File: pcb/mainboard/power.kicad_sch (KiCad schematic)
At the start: 0 parts

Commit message: - pcb: working on power supply
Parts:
- added C? (x3): 10uF, symbol Device:C
- added C? (x3): 22uF, Capacitor_SMD:C_0603_1608Metric, symbol Device:C
- added C? (x6): 100nF, symbol Device:C
- added C? (x3): 22uF, symbol Device:C
- added L? (x3): 470nH, symbol Device:L
- added R? (x3): 100R, Resistor_SMD:R_0402_1005Metric, symbol Device:R
- added R? (x2): 0R, Resistor_SMD:R_0402_1005Metric, symbol Device:R
- added R? (x2): 9.1K, Resistor_SMD:R_0402_1005Metric, symbol Device:R
- added R? (x3): 0.02R, Resistor_SMD:R_0805_2012Metric, symbol Device:R
- added U? (x3): RK809, symbol symbols:RK809
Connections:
- new net: C?.1, C?.1, C?.1, L?.2, R?.1, R?.1
- new net: C?.1, C?.1, U?.24 (VCC3), U?.66 (VCC4)
- new net: C?.2, U?.10 (VCC2), U?.11 (VCC1)
- new net: L?.2, U?.12 (SW1)
- new net: R?.2, R?.2, U?.13 (FB1)
- new net: C?.1, C?.2, R?.2, R?.2, U?.64 (FB4)
- new net: L?.1, U?.65 (SW4)
- new net: R?.2, R?.2, U?.8 (FB2)
- new net: L?.2, U?.9 (SW2)
- new net: C?.1, C?.1, C?.1, L?.1, R?.1, R?.2 (x2)
- new net: C?.1, C?.2, R?.1, R?.1, R?.2 (x2)
- new net GND: C?.1, C?.2, C?.2, C?.2, C?.2, C?.2, C?.2, C?.2, C?.2, C?.2, R?.1, R?.1

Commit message: - Upgrade KiCad to latest version - Working on PM circuits - Initial USB Type-C support - Initial support for LCD
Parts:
- removed R?: 9.1K, Resistor_SMD:R_0402_1005Metric, symbol Device:R
- removed R?: 0R, Resistor_SMD:R_0402_1005Metric, symbol Device:R
- added BT?: Battery, symbol Device:Battery
- added C? (x14): 100nF, Capacitor_SMD:C_0402_1005Metric, symbol Device:C
- added C? (x4): 1uF, symbol Device:C
- added C?: 100nF/16V, Capacitor_SMD:C_0402_1005Metric, symbol Device:C
- added C? (x2): 22uF, symbol Device:C
- added C? (x2): 22pF, Capacitor_SMD:C_0402_1005Metric, symbol Device:C
- added C? (x3): 10uF, symbol Device:C
- added C?: 1uF, Capacitor_SMD:C_0402_1005Metric, symbol Device:C
- added C? (x3): 100nF, symbol Device:C
- added L? (x2): 470nH, symbol Device:L
- added R?: 22K, Resistor_SMD:R_0402_1005Metric, symbol Device:R
- added R?: 120K/1%, Resistor_SMD:R_0402_1005Metric, symbol Device:R
- added R? (x5): 22R, Resistor_SMD:R_0402_1005Metric, symbol Device:R
- added R? (x13): 0.02R, Resistor_SMD:R_0805_2012Metric, symbol Device:R
- added R?: 140K, Resistor_SMD:R_0805_2012Metric, symbol Device:R
- added R?: 0.01R, Resistor_SMD:R_0402_1005Metric, symbol Device:R
- added R? (x2): 10K, Resistor_SMD:R_0402_1005Metric, symbol Device:R
- added R?: 220K, Resistor_SMD:R_0402_1005Metric, symbol Device:R
- added R?: 47K/1%, Resistor_SMD:R_0402_1005Metric, symbol Device:R
- added R?: 20K, Resistor_SMD:R_0402_1005Metric, symbol Device:R
- added SW? (x2): SW_Push, symbol Switch:SW_Push
- added Y?: 32.768K, Crystal:Crystal_SMD_TXC_9HT11-2Pin_2.0x1.2mm_HandSoldering, symbol Device:Crystal
- R?: value 0R -> 560R
- R?: value 9.1K -> DNP
- U?: value RK809 -> RK809-5
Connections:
- net GND: now also C?.2, C?.2, U?.47 (GNDREF), U?.63 (SNSN), U?.69 (EPAD), C?.1, C?.1, C?.1, C?.1, C?.1, C?.2, C?.2, C?.2, C?.2, C?.2, C?.2, C?.2, C?.2, C?.2, C?.2, C?.2, C?.2, C?.2, C?.2, C?.2, C?.2, C?.2, C?.2, C?.2, C?.2, C?.2, C?.2, C?.2, C?.2, C?.2, R?.2, R?.2, R?.2, R?.2, SW?.2, SW?.2
- net +3V3_SYS: now reaches C?.1, C?.1, U?.24 (VCC3), U?.66 (VCC4)
- net +3V3_SYS: now also C?.1, C?.2, C?.2, R?.2, R?.2, R?.2, R?.2, U?.10 (VCC2), U?.11 (VCC1), U?.13 (FB1), U?.22 (VCC5), U?.30 (VCC6), U?.4 (VCC7), U?.54 (VCC9), U?.57 (VCC8), U?.64 (FB4), C?.1, C?.1, C?.1, C?.1, C?.1
- net at U?.25 (SW3): now also L?.1
- net +DDR: now reaches U?.26 (VBUCK3)
- net +DDR: now also C?.1, R?.1, R?.2
- net at U?.27 (FB3): now also R?.1, R?.2
- net +GPU: now reaches U?.8 (FB2)
- net +GPU: now also C?.1, C?.2, R?.1, R?.2
- net +LOGIC: now reaches C?.1, C?.2, R?.1, R?.1, R?.2
- net at U?.1 (SCL): now also R?.2
- net at U?.2 (SDA): now also R?.2
- net +RTC: now reaches U?.45 (VCC_RTC)
- net +RTC: now also C?.1
- net at U?.46 (VREF): now also C?.2
- net PMIC_SLEEP_H: now reaches U?.49 (SLEEP)
- net at U?.50 (XIN): now also C?.2, Y?.2
- net at U?.51 (XOUT): now also C?.2, Y?.1
- net at U?.52 (PWRON): now also C?.1, R?.1
- net at U?.56 (BATDIV): now also R?.1, R?.1
- net PMIC_EXTEN: now reaches U?.60 (EXT_EN)
- net at U?.61 (VDC): now also C?.1, R?.1, R?.2
- net at U?.62 (SNSP): now also BT?.2 (-), R?.1
- net at U?.67 (RESETB): now also C?.2, R?.1, R?.2
- net at U?.68 (CLK32K): now also R?.2
- net PMIC_INT_L: now reaches U?.7 (INT)
- net at U?.20 (LDO3): now also C?.1, R?.1
- net at U?.21 (LDO2): now also C?.1, R?.1
- net at U?.23 (LDO1): now also C?.1, R?.1
- net at U?.28 (LDO4): now also C?.1, R?.1
- net at U?.29 (LDO5): now also C?.1, R?.1
- net at U?.3 (LDO7): now also C?.1, R?.1
- net at U?.31 (LDO6): now also C?.1, R?.1
- net at U?.5 (LDO8): now also C?.1, R?.1
- net at U?.53 (SW5): now also L?.1
- net at U?.55 (SWOUT1): now also C?.1, R?.1
- net at U?.58 (SWOUT2): now also C?.1, R?.1
- net +1V8: now reaches U?.59 (FB5)
- net +1V8: now also C?.1, R?.2
- net at U?.6 (LDO9): now also C?.1, R?.1
- new net: R?.2, SW?.1 (x2)
- new net: C?.1, C?.1, L?.2, R?.1 (x2)
- new net +0V9A: R?.2
- new net +0V9A_IMAGE: R?.2
- new net +0V9A_PMU: R?.2
- new net +12V: R?.1
- new net +1V8A: R?.2
- new net +1V8A_IMAGE: R?.2
- new net +1V8A_NPU: R?.2
- new net +3V3: R?.2
- new net +3V3_PMU: R?.2
- new net +BATT: BT?.1 (+), C?.2, R?.2
- new net +PMUIO1: R?.1
- new net +VCCIO_ACODEC: R?.2
- new net +VCCIO_WL: R?.1, R?.2
- new net +VSD: R?.2
- new net I2C_SCL_PMIC: R?.1
- new net I2C_SDA_PMIC: R?.1
- new net PMIC_32KOUT_WIFI: R?.1, R?.2
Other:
- note added: "2S Battery"
- note added: "DDR4 1.2V 62K/1% LPDDR4/X 1.1V 47K/1% DDR3 1.53V 110K/1% DDR3L 1.35V 82K/1% LPDDR3 1.2V 62K/1%"
- note added: "Todo: Make sure the power path allows the USB-C controller to be programmed during dead-battery condition"
- moved on the sheet: C?, L?, R?, U?A, U?B, U?C

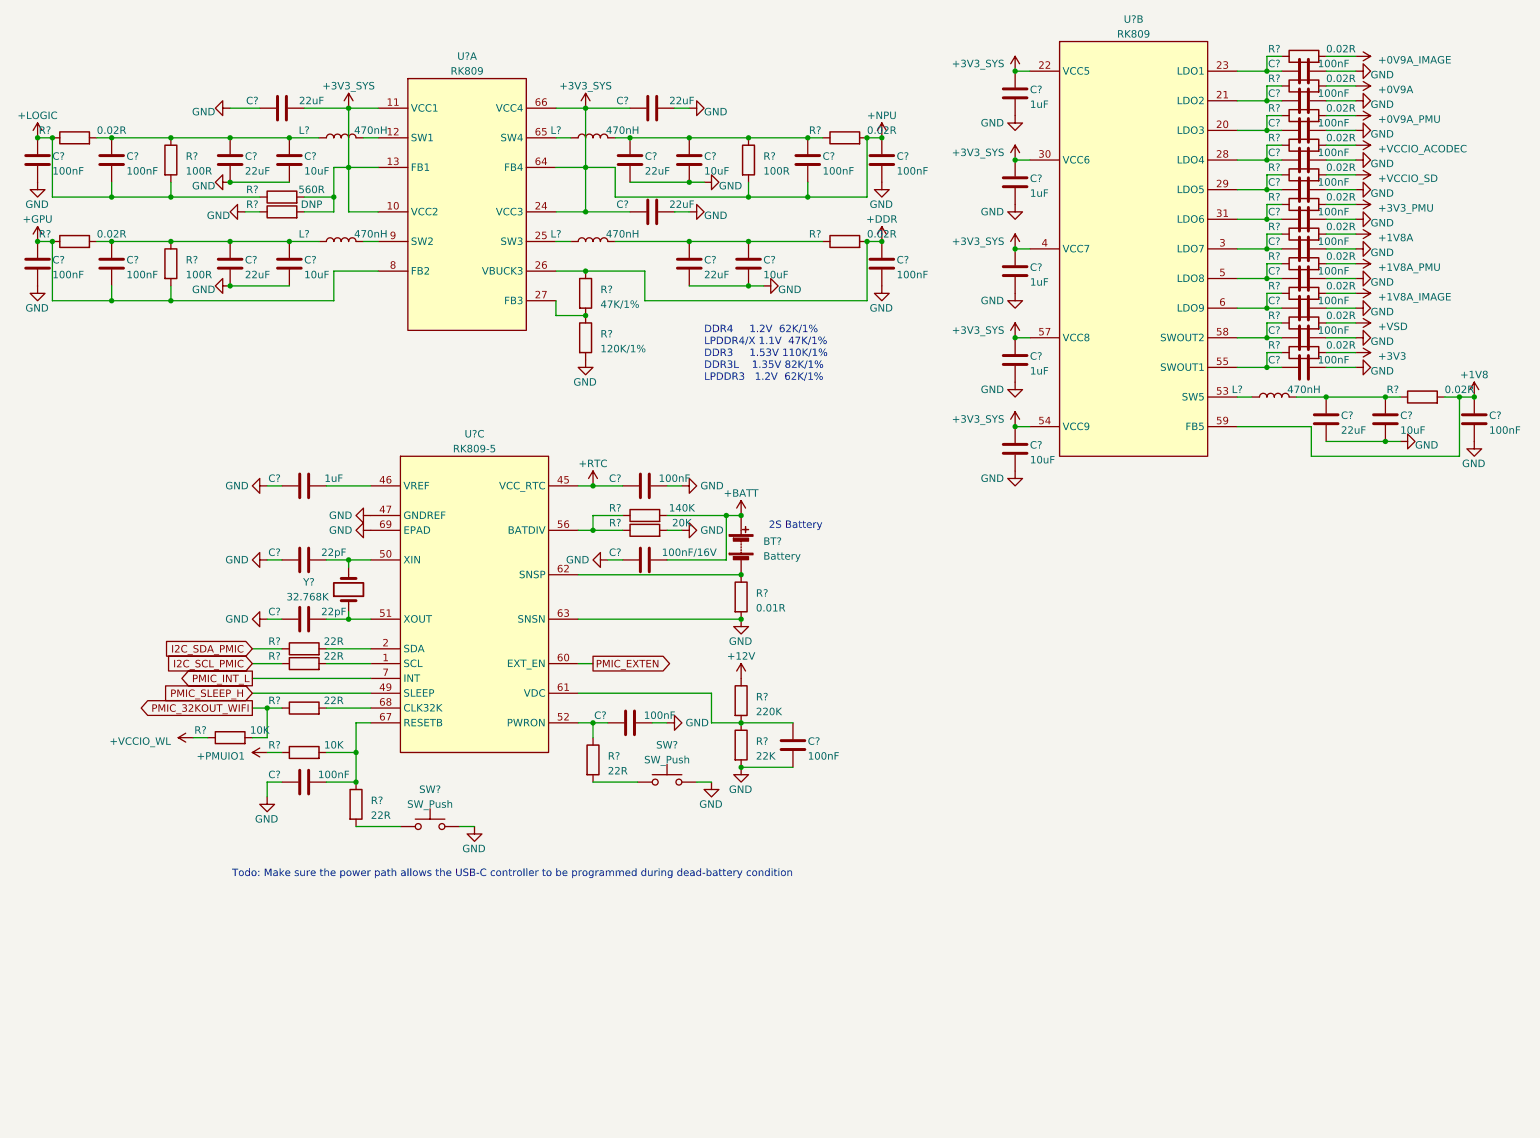
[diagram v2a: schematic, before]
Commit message: - pcb: switch to imx7 for the prototype
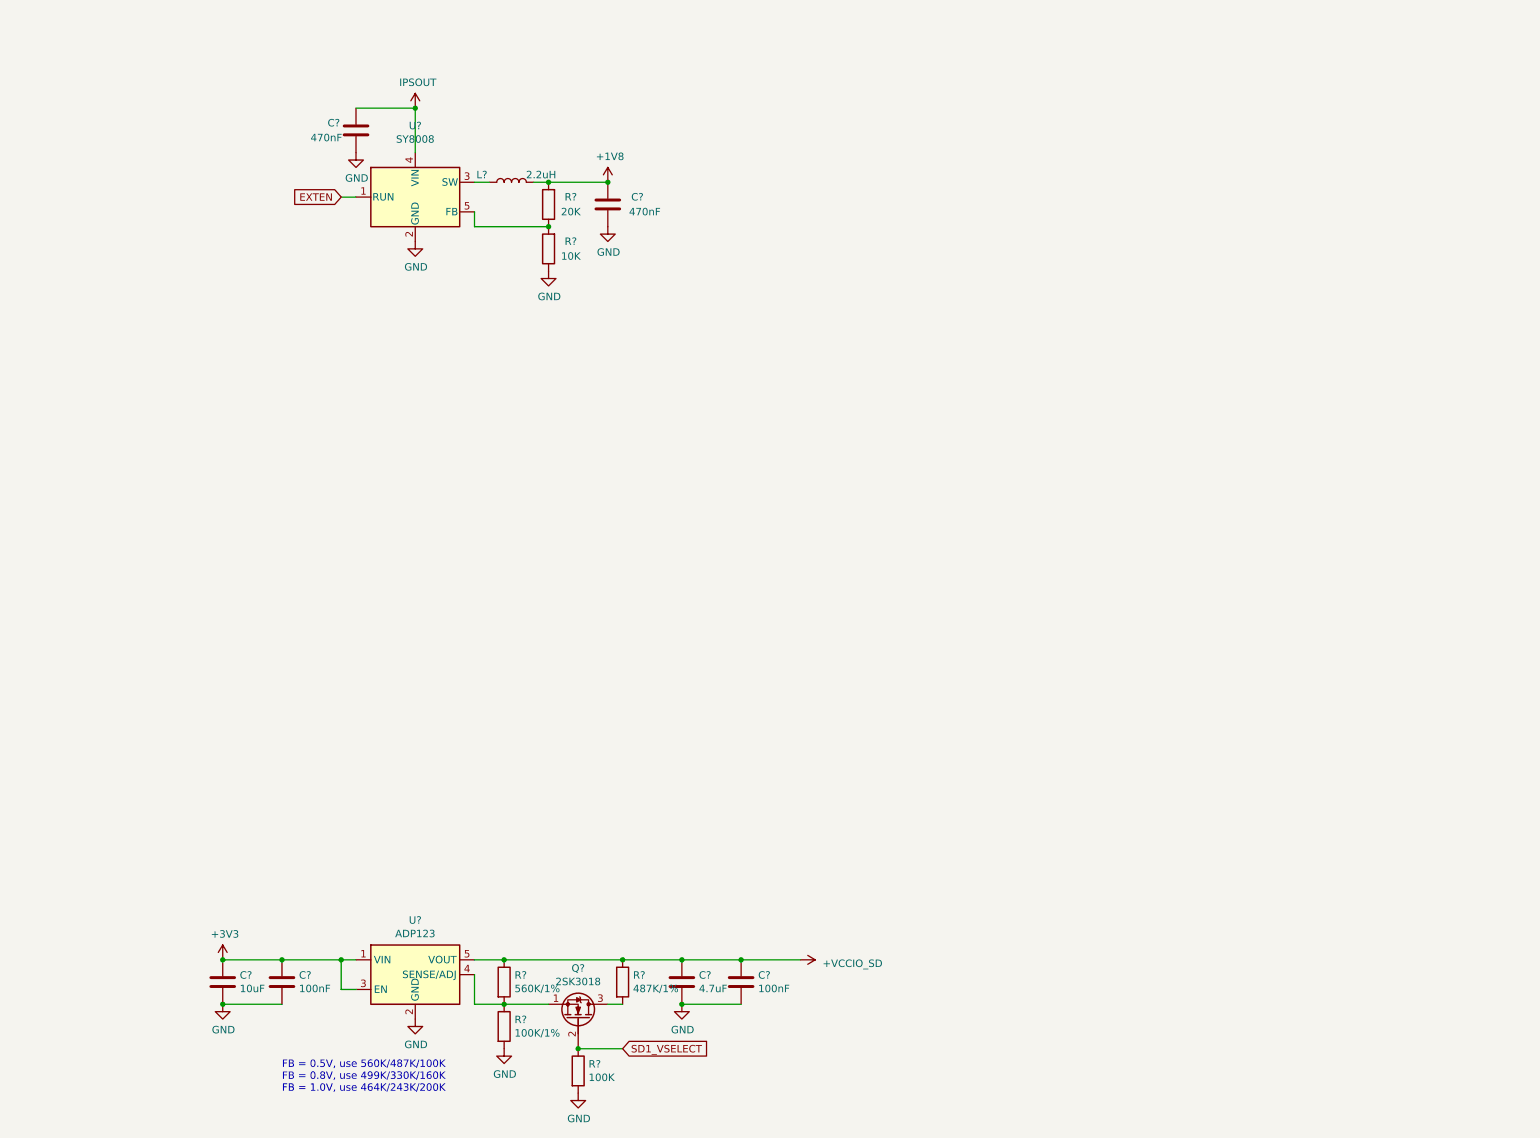
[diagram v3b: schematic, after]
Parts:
- removed BT?: Battery, symbol Device:Battery
- removed C? (x14): 100nF, Capacitor_SMD:C_0402_1005Metric, symbol Device:C
- removed C? (x6): 10uF, symbol Device:C
- removed C? (x4): 1uF, symbol Device:C
- removed C? (x3): 22uF, Capacitor_SMD:C_0603_1608Metric, symbol Device:C
- removed C?: 100nF/16V, Capacitor_SMD:C_0402_1005Metric, symbol Device:C
- removed C? (x9): 100nF, symbol Device:C
- removed C? (x5): 22uF, symbol Device:C
- removed C? (x2): 22pF, Capacitor_SMD:C_0402_1005Metric, symbol Device:C
- removed C?: 1uF, Capacitor_SMD:C_0402_1005Metric, symbol Device:C
- removed L? (x5): 470nH, symbol Device:L
- removed R?: 22K, Resistor_SMD:R_0402_1005Metric, symbol Device:R
- removed R?: 120K/1%, Resistor_SMD:R_0402_1005Metric, symbol Device:R
- removed R? (x3): 100R, Resistor_SMD:R_0402_1005Metric, symbol Device:R
- removed R? (x5): 22R, Resistor_SMD:R_0402_1005Metric, symbol Device:R
- removed R? (x16): 0.02R, Resistor_SMD:R_0805_2012Metric, symbol Device:R
- removed R?: 560R, Resistor_SMD:R_0402_1005Metric, symbol Device:R
- removed R?: 140K, Resistor_SMD:R_0805_2012Metric, symbol Device:R
- removed R?: 0.01R, Resistor_SMD:R_0402_1005Metric, symbol Device:R
- removed R? (x2): 10K, Resistor_SMD:R_0402_1005Metric, symbol Device:R
- removed R?: 220K, Resistor_SMD:R_0402_1005Metric, symbol Device:R
- removed R?: 47K/1%, Resistor_SMD:R_0402_1005Metric, symbol Device:R
- removed R?: 20K, Resistor_SMD:R_0402_1005Metric, symbol Device:R
- removed R?: DNP, Resistor_SMD:R_0402_1005Metric, symbol Device:R
- removed SW? (x2): SW_Push, symbol Switch:SW_Push
- removed U? (x2): RK809, symbol symbols:RK809
- removed U?: RK809-5, symbol symbols:RK809
- removed Y?: 32.768K, Crystal:Crystal_SMD_TXC_9HT11-2Pin_2.0x1.2mm_HandSoldering, symbol Device:Crystal
- added C?: 10uF, Capacitor_SMD:C_0603_1608Metric, symbol Device:C
- added C? (x2): 470nF, Capacitor_SMD:C_0402_1005Metric, symbol Device:C
- added C? (x2): 100nF, Capacitor_SMD:C_0402_1005Metric, symbol Device:C
- added C?: 4.7uF, Capacitor_SMD:C_0603_1608Metric, symbol Device:C
- added L?: 2.2uH, Inductor_SMD:L_Vishay_IHLP-1212, symbol Device:L
- added Q?: 2SK3018, Package_TO_SOT_SMD:SOT-23, symbol Device:Q_NMOS_SGD
- added R?: 100K/1%, Resistor_SMD:R_0603_1608Metric, symbol Device:R
- added R?: 10K, Resistor_SMD:R_0402_1005Metric, symbol Device:R
- added R?: 20K, Resistor_SMD:R_0402_1005Metric, symbol Device:R
- added R?: 100K, Resistor_SMD:R_0603_1608Metric, symbol Device:R
- added R?: 487K/1%, Resistor_SMD:R_0603_1608Metric, symbol Device:R
- added R?: 560K/1%, Resistor_SMD:R_0603_1608Metric, symbol Device:R
- added U?: SY8008, Package_TO_SOT_SMD:TSOT-23-5, symbol symbols:SY8008
- added U?: ADP123, Package_TO_SOT_SMD:TSOT-23-5, symbol Regulator_Linear:ADP7142AUJZ
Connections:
- net +1V8: now also C?.2, L?.2, R?.2
- net +3V3: now also C?.1, C?.1, U?.1 (VIN), U?.3 (EN)
- net +VCCIO_WL: now also C?.1, C?.1, R?.1, R?.1, U?.5 (VOUT)
- net GND: now also C?.1, C?.1, C?.2, C?.2, C?.2, C?.2, R?.1, R?.2, R?.2, U?.2 (GND), U?.2 (GND)
- new net: L?.1, U?.3 (SW)
- new net: R?.1, R?.2, U?.5 (FB)
- new net: Q?.1 (S), R?.1, R?.2, U?.4 (SENSE/ADJ)
- new net: Q?.3 (D), R?.2
- new net EXTEN: U?.1 (RUN)
- new net IPSOUT: C?.2, U?.4 (VIN)
- new net SD1_VSELECT: Q?.2 (G), R?.1
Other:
- note added: "FB = 0.5V, use 560K/487K/100K FB = 0.8V, use 499K/330K/160K FB = 1.0V, use 464K/243K/200K"
- note removed: "2S Battery"
- note removed: "DDR4 1.2V 62K/1% LPDDR4/X 1.1V 47K/1% DDR3 1.53V 110K/1% DDR3L 1.35V 82K/1% LPDDR3 1.2V 62K/1%"
- note removed: "Todo: Make sure the power path allows the USB-C controller to be programmed during dead-battery condition"

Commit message: - pcb: working on r0p1 sch
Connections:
- net EXTEN renamed PWR_1V8_EN
- net IPSOUT renamed +5V
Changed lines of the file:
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@@
     (effects (font (size 1.27 1.27)) (justify left bottom))
   )
-  (global_label "EXTEN" (shape input) (at 73.66 62.23 180)
+  (global_label "PWR_1V8_EN" (shape input) (at 73.66 62.23 180)
     (effects (font (size 1.27 1.27)) (justify right))
     (property "Intersheet References" "${INTERSHEET_REFS}" (id 0) (at -7.62 -107.95 0)
@@
     (pin "1")
   )
-  (symbol (lib_id "symbols:IPSOUT") (at 86.36 46.99 0) (unit 1)
-    (in_bom yes) (on_board yes)
+  (symbol (lib_id "power:+5V") (at 86.36 46.99 0) (unit 1)
+    (in_bom yes) (on_board yes) (fields_autoplaced)
     (property "Reference" "#PWR?" (id 0) (at 86.36 50.8 0)
       (effects (font (size 1.27 1.27)) hide)
     )
-    (property "Value" "IPSOUT" (id 1) (at 86.7918 42.5958 0))
+    (property "Value" "+5V" (id 1) (at 86.36 43.18 0))
     (property "Footprint" "" (id 2) (at 86.36 46.99 0)
       (effects (font (size 1.27 1.27)) hide)
